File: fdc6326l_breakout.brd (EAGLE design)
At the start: 19 x 14.9 mm, 7 parts, among them U1 FDC6326L

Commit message: b4 autoroute
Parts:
- moved C1 0.64 mm to (7.62, 6.99)
- moved R2 0.64 mm to (10.2, 6.99)
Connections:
- net N$3 renamed C!_R1
- net N$4 renamed R2
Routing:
- net VOUT: track 0.00 -> 13.3 mm, vias 0 -> 1
- net ONOFF: track 0.00 -> 6.86 mm, vias 0 -> 1
- net VCC: track 0.00 -> 3.80 mm
- net C!_R1: track 0.00 -> 1.48 mm
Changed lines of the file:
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@@
 <setting verticaltext="up"/>
 </settings>
-<grid distance="0.05" unitdist="inch" unit="inch" style="lines" multiple="1" display="no" altdistance="0.025" altunitdist="inch" altunit="inch"/>
+<grid distance="12.5" unitdist="mil" unit="mil" style="lines" multiple="1" display="yes" altdistance="0.025" altunitdist="inch" altunit="mil"/>
 <layers>
 <layer number="1" name="Top" color="4" fill="1" visible="yes" active="yes"/>
@@
 <attribute name="VALUE" x="10.795" y="11.43" size="1.27" layer="27" rot="R270"/>
 </element>
-<element name="C1" library="rcl" package="C0603" value="10pF" x="7.62" y="6.35" rot="MR90"/>
-<element name="R1" library="rcl" package="R0603" value="100k" x="7.62" y="10.16" rot="MR270"/>
-<element name="R2" library="rcl" package="R0603" value="1k" x="10.16" y="6.35" rot="MR270"/>
-<element name="OFF_PD" library="rcl" package="R0603" value="10k" x="10.16" y="10.16" rot="MR90"/>
+<element name="C1" library="rcl" package="C0603" value="10pF" x="7.62" y="6.985" smashed="yes" rot="MR90">
+<attribute name="NAME" x="5.715" y="4.445" size="1.27" layer="26" rot="MR90"/>
+</element>
+<element name="R1" library="rcl" package="R0603" value="100k" x="7.62" y="10.16" smashed="yes" rot="MR270">
+<attribute name="NAME" x="6.985" y="12.7" size="1.27" layer="26" rot="MR270"/>
+</element>
+<element name="R2" library="rcl" package="R0603" value="1k" x="10.16" y="6.985" smashed="yes" rot="MR270">
+<attribute name="NAME" x="12.065" y="6.985" size="1.27" layer="26" rot="MR270"/>
+</element>
+<element name="OFF_PD" library="rcl" package="R0603" value="10k" x="10.16" y="10.16" smashed="yes" rot="MR90">
+<attribute name="NAME" x="16.51" y="11.43" size="1.27" layer="26" rot="MR90"/>
+</element>
 </elements>
 <signals>
@@
 <contactref element="U1" pad="4"/>
 <contactref element="R1" pad="1"/>
+<wire x1="3.81" y1="10.16" x2="7.5946" y2="9.8298" width="0.4064" layer="1"/>
 <wire x1="7.5946" y1="9.8298" x2="7.62" y2="11.01" width="0" layer="19" extent="1-16"/>
-<wire x1="3.81" y1="10.16" x2="7.5946" y2="9.8298" width="0" layer="19" extent="1-1"/>
 </signal>
 <signal name="GND">
@@
 <contactref element="U1" pad="5"/>
 <contactref element="OFF_PD" pad="1"/>
-<wire x1="7.5946" y1="8.89" x2="10.16" y2="9.31" width="0" layer="19" extent="1-16"/>
-<wire x1="3.81" y1="7.62" x2="7.5946" y2="8.89" width="0" layer="19" extent="1-1"/>
+<wire x1="3.81" y1="7.62" x2="5.3975" y2="8.89" width="0.254" layer="1"/>
+<wire x1="5.3975" y1="8.89" x2="7.5946" y2="8.89" width="0.254" layer="1"/>
+<wire x1="7.5946" y1="8.89" x2="8.89" y2="8.89" width="0.254" layer="1"/>
+<via x="8.89" y="8.89" extent="1-16" drill="0.3048"/>
+<wire x1="8.89" y1="8.89" x2="10.16" y2="9.31" width="0.254" layer="16"/>
 </signal>
 <signal name="VOUT">
@@
 <contactref element="U1" pad="3"/>
 <contactref element="C1" pad="1"/>
-<wire x1="10.1854" y1="9.8298" x2="13.97" y2="10.16" width="0" layer="19" extent="1-1"/>
-<wire x1="10.1854" y1="8.89" x2="10.1854" y2="9.8298" width="0" layer="19" extent="1-1"/>
-<wire x1="7.62" y1="5.5" x2="10.1854" y2="8.89" width="0" layer="19" extent="1-16"/>
-</signal>
-<signal name="N$3">
+<wire x1="10.1854" y1="8.89" x2="10.1854" y2="9.8298" width="0.4064" layer="1"/>
+<wire x1="10.1854" y1="9.8298" x2="13.97" y2="10.16" width="0.4064" layer="1"/>
+<wire x1="10.1854" y1="8.89" x2="11.7475" y2="8.89" width="0.254" layer="1"/>
+<wire x1="11.7475" y1="8.89" x2="11.7475" y2="6.0325" width="0.254" layer="1"/>
+<wire x1="11.7475" y1="6.0325" x2="8.89" y2="6.0325" width="0.254" layer="1"/>
+<via x="8.89" y="6.0325" extent="1-16" drill="0.3048"/>
+<wire x1="8.89" y1="6.0325" x2="7.62" y2="6.135" width="0.254" layer="16"/>
+</signal>
+<signal name="C!_R1">
 <contactref element="R1" pad="2"/>
 <contactref element="C1" pad="2"/>
 <contactref element="U1" pad="6"/>
-<wire x1="7.5946" y1="7.9502" x2="7.62" y2="9.31" width="0" layer="19" extent="1-16"/>
-<wire x1="7.62" y1="7.2" x2="7.5946" y2="7.9502" width="0" layer="19" extent="1-16"/>
-</signal>
-<signal name="N$4">
+<wire x1="7.62" y1="9.31" x2="7.62" y2="7.835" width="0.254" layer="16"/>
+<wire x1="7.5946" y1="7.9502" x2="7.62" y2="7.835" width="0" layer="19" extent="1-16"/>
+</signal>
+<signal name="R2">
 <contactref element="U1" pad="1"/>
 <contactref element="R2" pad="1"/>
-<wire x1="10.16" y1="7.2" x2="10.1854" y2="7.9502" width="0" layer="19" extent="1-16"/>
+<via x="10.16" y="7.9375" extent="1-16" drill="0.3048"/>
+<wire x1="10.16" y1="7.9375" x2="10.1854" y2="7.9502" width="0" layer="19" extent="1-1"/>
+<wire x1="10.16" y1="7.835" x2="10.1854" y2="7.9502" width="0" layer="19" extent="1-16"/>
+</signal>
+<signal name="C1_R1">
+<via x="7.62" y="7.9375" extent="1-16" drill="0.3048"/>
 </signal>
 </signals>

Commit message: routed
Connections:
- removed net C!_R1: C1.2, R1.2, U1.6
- new net C1_R1: C1.2, R1.2, U1.6
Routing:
- net VCC: track 3.80 -> 7.98 mm
- net C1_R1: track 0.00 -> 1.52 mm
- net C!_R1: track 1.48 -> 0.00 mm
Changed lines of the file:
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@@
 <autorouter>
 <pass name="Default">
-<param name="RoutingGrid" value="50mil"/>
+<param name="RoutingGrid" value="4mil"/>
 <param name="tpViaShape" value="round"/>
 <param name="PrefDir.1" value="|"/>
@@
 <contactref element="R1" pad="1"/>
 <wire x1="3.81" y1="10.16" x2="7.5946" y2="9.8298" width="0.4064" layer="1"/>
-<wire x1="7.5946" y1="9.8298" x2="7.62" y2="11.01" width="0" layer="19" extent="1-16"/>
+<wire x1="7.4168" y1="10.7696" x2="7.62" y2="10.9728" width="0.1524" layer="16"/>
+<wire x1="5.1816" y1="10.7696" x2="7.4168" y2="10.7696" width="0.1524" layer="16"/>
+<wire x1="4.572" y1="10.16" x2="5.1816" y2="10.7696" width="0.1524" layer="16"/>
+<wire x1="3.81" y1="10.16" x2="4.572" y2="10.16" width="0.1524" layer="16"/>
+<wire x1="7.62" y1="10.9728" x2="7.62" y2="11.01" width="0.1524" layer="16"/>
 </signal>
 <signal name="GND">
@@
 <wire x1="8.89" y1="6.0325" x2="7.62" y2="6.135" width="0.254" layer="16"/>
 </signal>
-<signal name="C!_R1">
-<contactref element="R1" pad="2"/>
-<contactref element="C1" pad="2"/>
-<contactref element="U1" pad="6"/>
-<wire x1="7.62" y1="9.31" x2="7.62" y2="7.835" width="0.254" layer="16"/>
-<wire x1="7.5946" y1="7.9502" x2="7.62" y2="7.835" width="0" layer="19" extent="1-16"/>
-</signal>
 <signal name="R2">
 <contactref element="U1" pad="1"/>
 <contactref element="R2" pad="1"/>
 <via x="10.16" y="7.9375" extent="1-16" drill="0.3048"/>
-<wire x1="10.16" y1="7.9375" x2="10.1854" y2="7.9502" width="0" layer="19" extent="1-1"/>
-<wire x1="10.16" y1="7.835" x2="10.1854" y2="7.9502" width="0" layer="19" extent="1-16"/>
+<wire x1="10.16" y1="7.9248" x2="10.16" y2="7.9375" width="0.1524" layer="1"/>
+<wire x1="10.16" y1="7.9248" x2="10.1854" y2="7.9502" width="0.1524" layer="1"/>
+<wire x1="10.16" y1="7.9375" x2="10.16" y2="7.835" width="0.1524" layer="16"/>
 </signal>
 <signal name="C1_R1">
 <via x="7.62" y="7.9375" extent="1-16" drill="0.3048"/>
+<contactref element="R1" pad="2"/>
+<contactref element="C1" pad="2"/>
+<contactref element="U1" pad="6"/>
+<wire x1="7.62" y1="9.31" x2="7.62" y2="7.9375" width="0.254" layer="16"/>
+<wire x1="7.62" y1="7.9375" x2="7.62" y2="7.9248" width="0.254" layer="16"/>
+<wire x1="7.62" y1="7.9248" x2="7.62" y2="7.835" width="0.254" layer="16"/>
+<wire x1="7.62" y1="7.9248" x2="7.62" y2="7.9375" width="0.1524" layer="1"/>
+<wire x1="7.62" y1="7.9248" x2="7.5946" y2="7.9502" width="0.1524" layer="1"/>
 </signal>
 </signals>

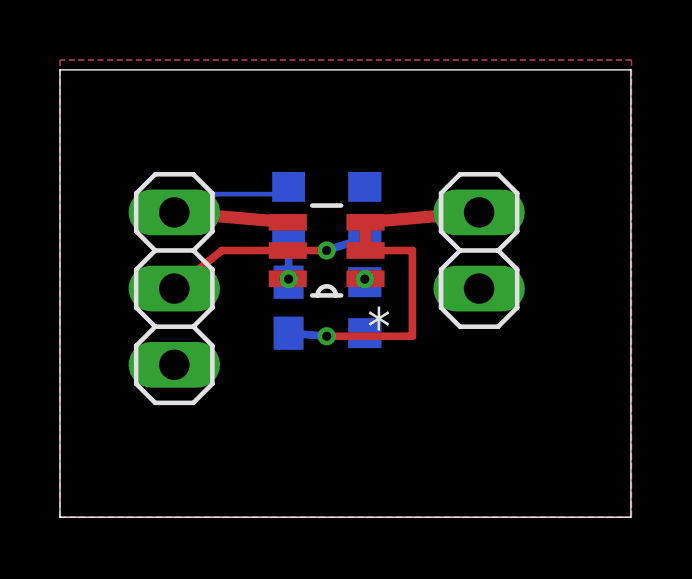
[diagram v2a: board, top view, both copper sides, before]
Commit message: make the board smaller
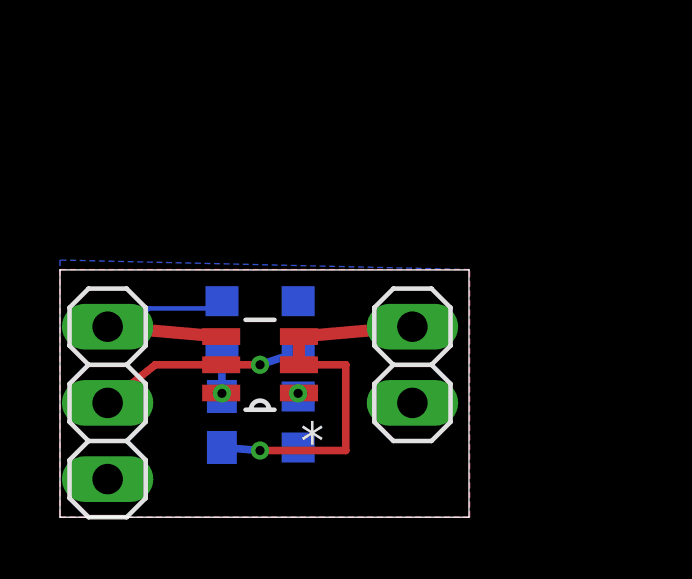
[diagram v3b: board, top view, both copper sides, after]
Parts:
- removed OFF_PD: 10k, rcl:R0603
- added PD: 10k, rcl:R0603
- moved C1 4.41 mm to (5.40, 3.17)
- moved JP1 4.41 mm to (1.59, 3.81)
- moved JP2 4.41 mm to (11.7, 5.08)
- moved R1 4.41 mm to (5.40, 6.35)
- moved R2 4.41 mm to (7.94, 3.17)
- moved U1 4.41 mm to (6.67, 5.08)
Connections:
- net GND: now also PD.2; no longer OFF_PD.2
- net ONOFF: now also PD.1; no longer OFF_PD.1
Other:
- board size 19 x 14.9 mm -> 13.6 x 8.2 mm
